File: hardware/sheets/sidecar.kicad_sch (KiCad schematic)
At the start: 3 parts, among them J1 ISA 8-bit (60p)

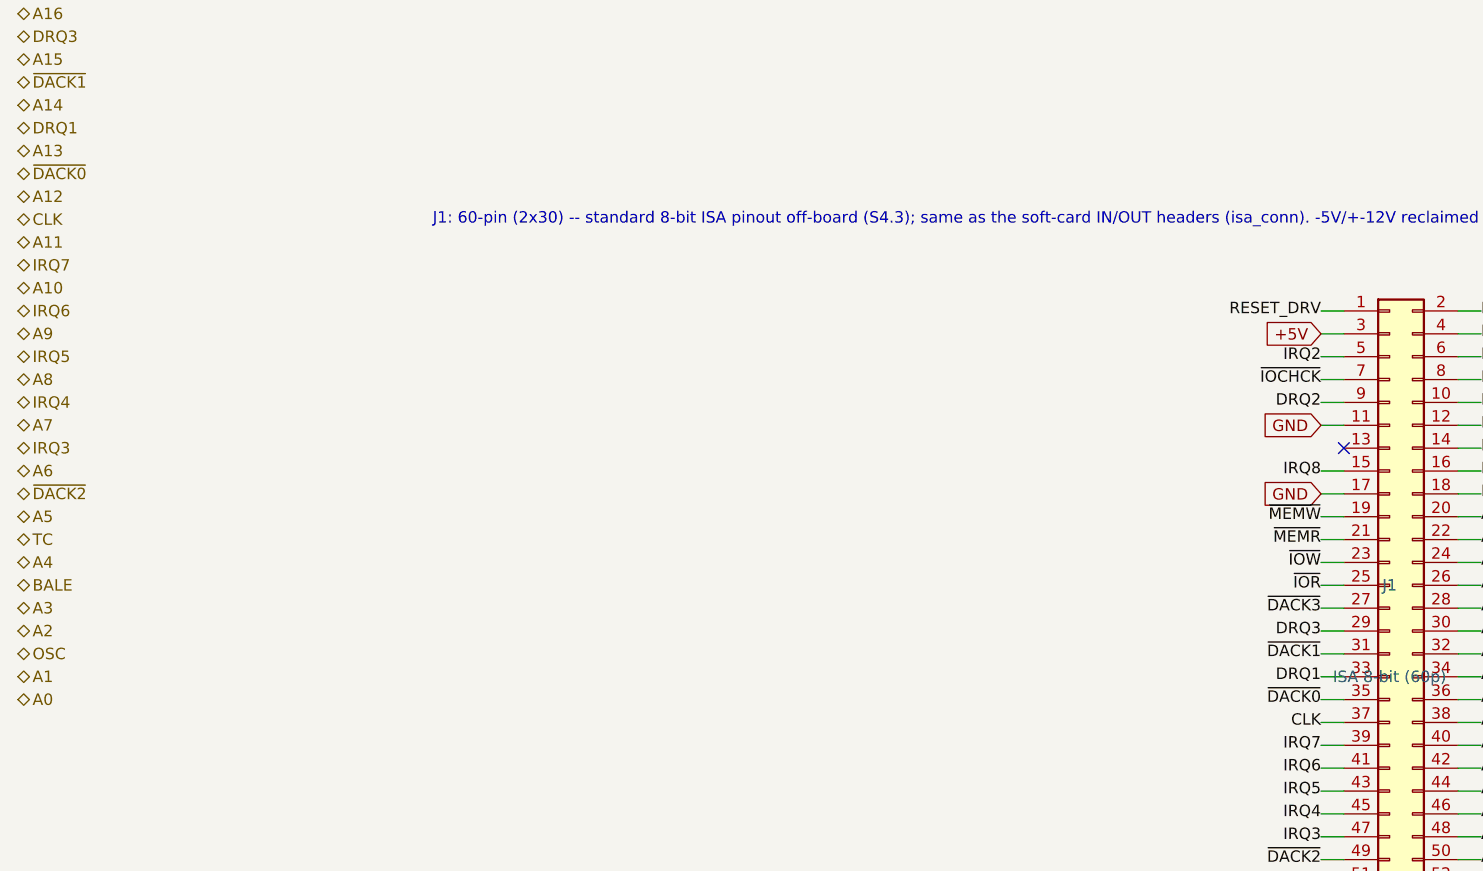
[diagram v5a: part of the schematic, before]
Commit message: Drive ISA REFRESH# from the Bus MCU for DRAM-based cards
Pin 35 (DACK0/REFRESH#) net renamed ~{DACK0} -> ~{REFRESH} in isa_conn and is now
an active Bus MCU output (GPIO47, reclaimed from the redundant raw-~WR sense -- the
MCU tracks writes via the gated MEMW/IOW). Driven from the internal ~15us refresh
timer (same source as the 0x61-bit-4 toggle); a refresh cycle reuses the bus-master
engine to walk the row address on A0-A7 + pulse MEMR#, so DRAM ISA cards see a
standard refresh. ~{REFRESH} added to the Bus MCU interface. Verified it ties
sidecar<->Bus MCU and passes through J_IN<->J_OUT on every dev card; zero
structural ERC on motherboard and all five cards.

Co-Authored-By: Claude Opus 4.8 (1M context) <noreply@anthropic.com>
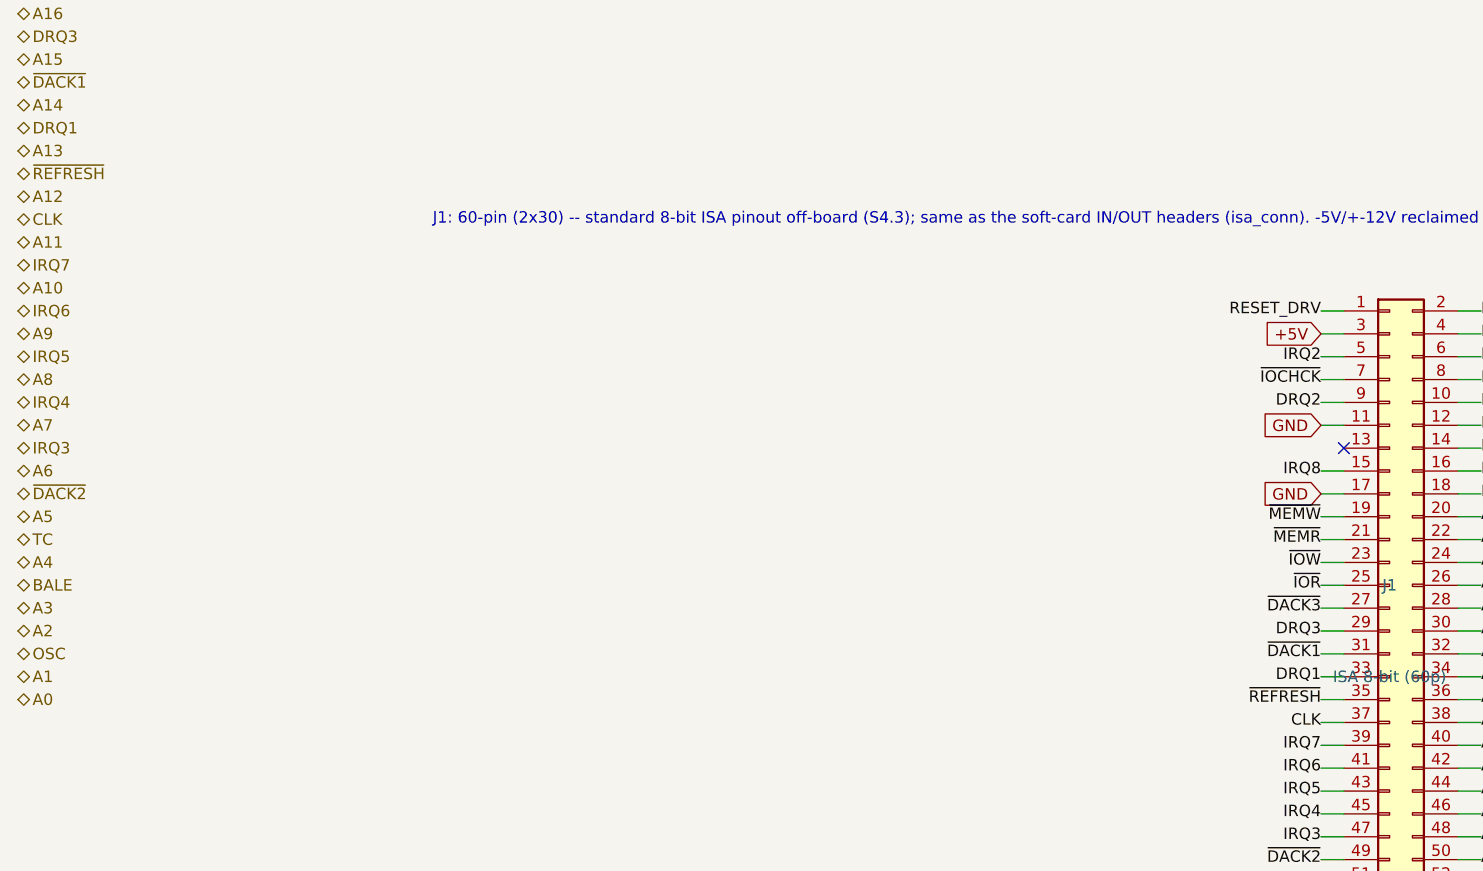
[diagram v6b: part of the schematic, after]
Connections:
- net ~{DACK0} renamed ~{REFRESH}
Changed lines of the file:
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@@
 		)
 	)
-	(hierarchical_label "~{DACK0}"
+	(hierarchical_label "~{REFRESH}"
 		(shape bidirectional)
 		(at 25.4 101.6 0)
@@
 		)
 	)
-	(label "~{DACK0}"
+	(label "~{REFRESH}"
 		(at 170.18 160.02 180)
 		(effects
@@
 		(instances
 			(project "mini-xt"
-				(path "/9602cc72-403c-4cc6-86da-e35dd0751fe2/907989ed-05aa-463a-9ce3-8ab9d4358248"
+				(path "/442cfbd8-63ab-49e7-b08c-2cb3161d8599/bad3514e-e676-4685-ae84-d10275f663f5"
 					(reference "J1201")
 					(unit 1)
@@
 		(instances
 			(project "mini-xt"
-				(path "/9602cc72-403c-4cc6-86da-e35dd0751fe2/907989ed-05aa-463a-9ce3-8ab9d4358248"
+				(path "/442cfbd8-63ab-49e7-b08c-2cb3161d8599/bad3514e-e676-4685-ae84-d10275f663f5"
 					(reference "C1201")
 					(unit 1)
@@
 		(instances
 			(project "mini-xt"
-				(path "/9602cc72-403c-4cc6-86da-e35dd0751fe2/907989ed-05aa-463a-9ce3-8ab9d4358248"
+				(path "/442cfbd8-63ab-49e7-b08c-2cb3161d8599/bad3514e-e676-4685-ae84-d10275f663f5"
 					(reference "C1202")
 					(unit 1)
